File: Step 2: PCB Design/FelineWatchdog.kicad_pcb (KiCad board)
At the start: 2 copper layers, 38 x 65 mm, 33 parts, among them J1 USB_C_Receptacle_PowerOnly_6P, J12 Conn_01x04_Socket, J2 Conn_01x02_Socket, J3 Conn_01x02_Pin, Q2 FS8205A, SW1 RESET, U1 AMS1117-3.3, U3 TP4056, U4 DW01A, U5 ESP-32S

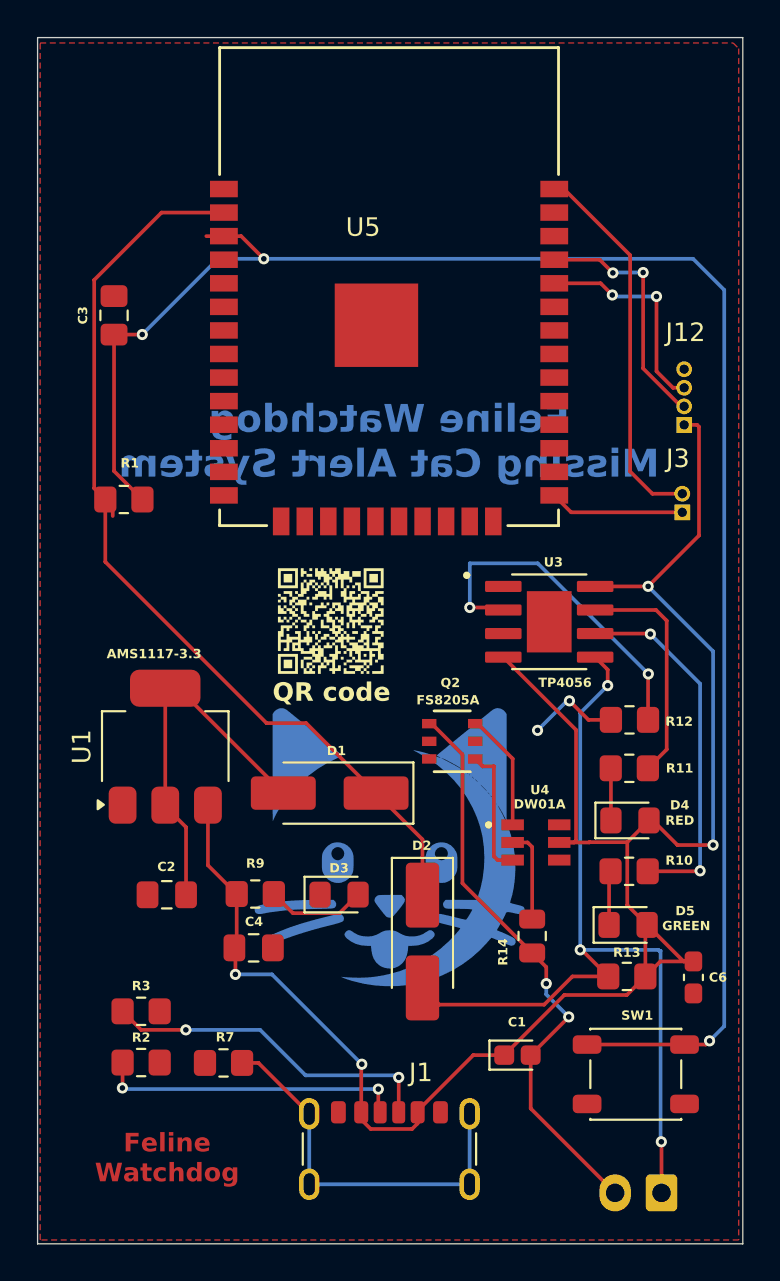
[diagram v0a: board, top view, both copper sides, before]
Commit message: Switch to 4-layer PCB stackup with dedicated power and ground planes Inner layers ensure stable power delivery, improved signal integrity, and reduced EMI.
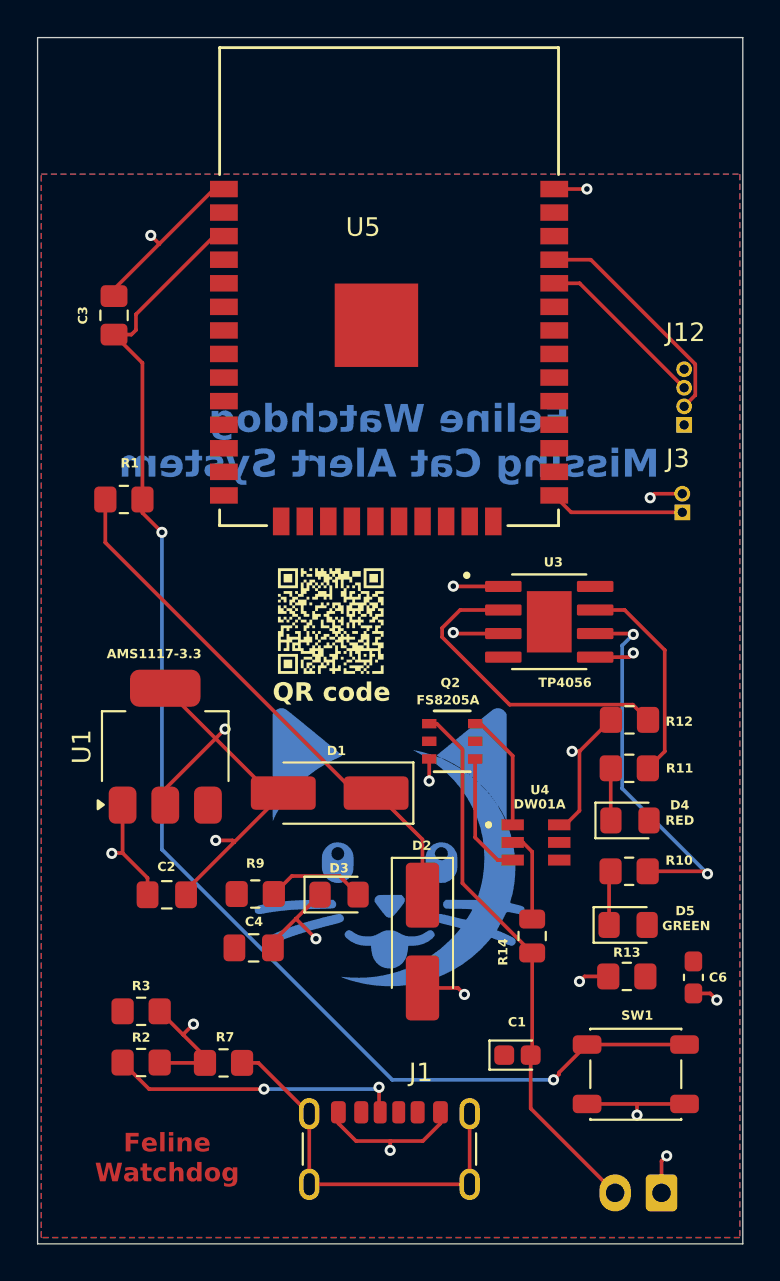
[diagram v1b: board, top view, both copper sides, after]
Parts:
- renumbered G*** to G1, G*** to G2
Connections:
- J3 pad 2: /ESP32 GND -> GND
- U5 pad 38: /ESP32 GND -> GND
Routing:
- net +5V: track 106.0 -> 0.00 mm, vias 4 -> 0
- net GND: track 5.88 -> 73.2 mm, vias 2 -> 13
- net BATT +: track 47.2 -> 8.32 mm, vias 3 -> 4
- net Net-(U5-EN): track 96.2 -> 71.6 mm, vias 3 -> 2
- net Net-(D1-K): track 51.1 -> 29.0 mm
- net /ESP32 GND: track 20.5 -> 0.00 mm
- net Net-(J1-CC2): track 18.2 -> 0.00 mm, vias 2 -> 0
- net +3.3V: track 20.3 -> 22.8 mm, vias 0 -> 2
- net /ESP32 RX: track 11.7 -> 9.33 mm, vias 2 -> 0
- net Net-(U3-PROG): track 18.8 -> 17.1 mm, vias 2 -> 0
- net BATT -: track 31.2 -> 29.7 mm, vias 2 -> 0
- net Net-(U3-~{CHRG}): track 12.5 -> 11.4 mm
- net /ESP32 TX: track 13.3 -> 12.5 mm, vias 2 -> 0
- net Net-(U3-~{STDBY}): track 19.7 -> 20.4 mm
- net Net-(J1-CC1): track 16.5 -> 15.8 mm
- added copper zone on In1.Cu, net +3.3V
- added copper zone on F.Cu, net +5V
- added copper zone on B.Cu, net BATT +
- added copper zone on In2.Cu, net GND
- removed copper zone on F.Cu, net GND
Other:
- copper layers 2 -> 4
